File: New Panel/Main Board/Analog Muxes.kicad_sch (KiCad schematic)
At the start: 242 parts, among them J10 Conn_02x07_Odd_Even, J11 Conn_02x07_Odd_Even, J12 Conn_02x07_Odd_Even, J13 Conn_01x03_Pin, J14 Conn_01x03_Pin, J15 Conn_01x03_Pin, J16 Conn_01x03_Pin, J17 Conn_01x03_Pin, J18 Conn_01x03_Pin, J19 Conn_01x03_Pin, J20 Conn_01x03_Pin, J21 Conn_01x03_Pin, J22 Conn_01x03_Pin, J23 Conn_01x03_Pin, J24 Conn_01x03_Pin, J25 Conn_01x03_Pin, J26 Conn_01x03_Pin, J27 Conn_01x03_Pin, J28 Conn_01x03_Pin, J29 Conn_01x03_Pin, J30 Conn_01x03_Pin, J31 Conn_01x03_Pin, J32 Conn_01x03_Pin, J33 Conn_01x03_Pin, J34 Conn_01x03_Pin, J35 Conn_01x03_Pin, J36 Conn_01x03_Pin, J37 Conn_01x03_Pin, J38 Conn_01x03_Pin, J39 Conn_01x03_Pin, J40 Conn_01x03_Pin, J41 Conn_01x03_Pin, J42 Conn_01x03_Pin, J43 Conn_01x03_Pin, J44 Conn_01x03_Pin, J45 Conn_01x03_Pin, J46 Conn_01x03_Pin, J47 Conn_01x03_Pin, J48 Conn_01x03_Pin, J49 Conn_01x03_Pin, J5 Conn_02x07_Odd_Even, J50 Conn_01x03_Pin, J51 Conn_01x03_Pin, J52 Conn_01x03_Pin, J53 Conn_01x03_Pin, J54 Conn_01x03_Pin, J55 Conn_01x03_Pin, J56 Conn_01x03_Pin, J57 Conn_01x03_Pin, J58 Conn_01x03_Pin, J59 Conn_01x03_Pin, J6 Conn_02x07_Odd_Even, J60 Conn_01x03_Pin, J61 Conn_02x07_Odd_Even, J62 Conn_02x07_Odd_Even, J63 Conn_02x07_Odd_Even, J64 Conn_02x07_Odd_Even, J65 Conn_01x03_Pin, J66 Conn_01x03_Pin, J67 Conn_01x03_Pin, J68 Conn_01x03_Pin, J69 Conn_01x03_Pin, J7 Conn_02x07_Odd_Even, J70 Conn_01x03_Pin, J71 Conn_01x03_Pin, J72 Conn_01x03_Pin, J73 Conn_01x03_Pin, J74 Conn_01x03_Pin, J75 Conn_01x03_Pin, J76 Conn_01x03_Pin, J77 Conn_01x03_Pin, J78 Conn_01x03_Pin, J79 Conn_01x03_Pin, J8 Conn_02x07_Odd_Even, J80 Conn_01x03_Pin, J81 Conn_02x07_Odd_Even, J82 Conn_02x07_Odd_Even, J83 Conn_02x07_Odd_Even, J84 Conn_02x07_Odd_Even, J9 Conn_02x07_Odd_Even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

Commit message: adjusted schematic and started PCB Work
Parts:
- removed C12, C13, C14, C15, C16, C17, C18, C19: 10uF, Capacitor_SMD:C_0603_1608Metric_Pad1.08x0.95mm_HandSolder, symbol Device:C
- removed J45, J46, J47, J48, J49, J50, J51, J52, J53, J54, J55, J56, J57, J58, J59, J60, J65, J66, J67, J68, J69, J70, J71, J72, J73, J74, J75, J76, J77, J78, J79, J80: Conn_01x03_Pin, Connector_JST:JST_PH_B3B-PH-K_1x03_P2.00mm_Vertical, symbol Connector:Conn_01x03_Pin
- removed J61, J62, J63, J64, J81, J82, J83, J84: Conn_02x07_Odd_Even, Connector_IDC:IDC-Header_2x07_P2.54mm_Vertical, symbol Connector_Generic:Conn_02x07_Odd_Even
- removed R100, R101, R102, R103, R104, R105, R106, R107, R108, R109, R110, R111, R112, R113, R114, R115, R116, R117, R118, R119, R120, R121, R122, R123, R124, R125, R126, R127, R128, R129, R66, R67, R68, R69, R70, R71, R72, R73, R74, R75, R76, R77, R78, R79, R80, R81, R82, R83, R84, R85, R86, R87, R88, R89, R90, R91, R92, R93, R94, R95, R96, R97, R98, R99: 10K, Resistor_SMD:R_0603_1608Metric, symbol Device:R
- removed U11, U12, U13, U14, U15, U16, U17, U18: Analog_MUX_CD4067BPWR, New Panel Parts:24-TSSOP_(4.4mm), symbol New_Panel_Parts:Analog_MUX_CD4067BPWR
- added D65, D66, D67, D68, D69, D70, D71, D72, D73, D74, D75, D76, D77, D78, D79, D80, D81, D82, D83, D84, D85, D86, D87, D88, D89, D90, D91, D92, D93, D94, D95, D96: DESD5V0S1BA-7, Diode_SMD:D_SOD-323, symbol Diode:SD05_SOD323
- added TP1, TP2, TP3, TP4, TP5, TP6, TP7, TP8: TestPoint, Connector_Pin:Pin_D1.0mm_L10.0mm, symbol Connector:TestPoint
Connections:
- net SW0_0: now also D65.1 (A1)
- net SW0_1: now also J44.2 (Pin_2), D96.1 (A1); no longer J41.2 (Pin_2), U10.9 (CHANNELIN/OUT0)
- net SW10_0: now also D75.1 (A1)
- net SW10_1: now also J34.2 (Pin_2), D86.1 (A1); no longer J35.2 (Pin_2), U10.21 (CHANNELIN/OUT10)
- net SW11_0: now also D76.1 (A1)
- net SW11_1: now also J33.2 (Pin_2), D85.1 (A1); no longer J31.2 (Pin_2), U10.20 (CHANNELIN/OUT11)
- net SW12_0: now also D77.1 (A1)
- net SW12_1: now also J32.2 (Pin_2), D84.1 (A1); no longer J44.2 (Pin_2), U10.19 (CHANNELIN/OUT12)
- net SW13_0: now also D78.1 (A1)
- net SW13_1: now also J31.2 (Pin_2), D83.1 (A1); no longer J40.2 (Pin_2), U10.18 (CHANNELIN/OUT13)
- net SW14_0: now also D79.1 (A1)
- net SW14_1: now also J30.2 (Pin_2), D82.1 (A1); no longer J36.2 (Pin_2), U10.17 (CHANNELIN/OUT14)
- net SW15_0: now also D80.1 (A1)
- net SW15_1: now also J29.2 (Pin_2), D81.1 (A1); no longer J32.2 (Pin_2), U10.16 (CHANNELIN/OUT15)
- net SW1_0: now also D66.1 (A1)
- net SW1_1: now also J43.2 (Pin_2), D95.1 (A1); no longer J37.2 (Pin_2), U10.8 (CHANNELIN/OUT1)
- net SW2_0: now also D67.1 (A1)
- net SW2_1: now also J42.2 (Pin_2), D94.1 (A1); no longer J33.2 (Pin_2), U10.7 (CHANNELIN/OUT2)
- net SW3_0: now also D68.1 (A1)
- net SW3_1: now also J41.2 (Pin_2), D93.1 (A1); no longer J29.2 (Pin_2), U10.6 (CHANNELIN/OUT3)
- net SW4_0: now also D69.1 (A1)
- net SW4_1: now also J40.2 (Pin_2), D92.1 (A1); no longer J42.2 (Pin_2), U10.5 (CHANNELIN/OUT4)
- net SW5_0: now also D70.1 (A1)
- net SW5_1: now also J39.2 (Pin_2), D91.1 (A1); no longer J38.2 (Pin_2), U10.4 (CHANNELIN/OUT5)
- net SW6_0: now also D71.1 (A1)
- net SW6_1: now also J38.2 (Pin_2), D90.1 (A1); no longer J34.2 (Pin_2), U10.3 (CHANNELIN/OUT6)
- net SW7_0: now also D72.1 (A1)
- net SW7_1: now also J37.2 (Pin_2), D89.1 (A1); no longer J30.2 (Pin_2), U10.2 (CHANNELIN/OUT7)
- net SW8_0: now also D73.1 (A1)
- net SW8_1: now also J36.2 (Pin_2), D88.1 (A1); no longer J43.2 (Pin_2), U10.23 (CHANNELIN/OUT8)
- net SW9_0: now also D74.1 (A1)
- net SW9_1: now also J35.2 (Pin_2), D87.1 (A1); no longer J39.2 (Pin_2), U10.22 (CHANNELIN/OUT9)
- net VSS: now also D65.2 (A2), D66.2 (A2), D67.2 (A2), D68.2 (A2), D69.2 (A2), D70.2 (A2), D71.2 (A2), D72.2 (A2), D73.2 (A2), D74.2 (A2), D75.2 (A2), D76.2 (A2), D77.2 (A2), D78.2 (A2), D79.2 (A2), D80.2 (A2), D81.2 (A2), D82.2 (A2), D83.2 (A2), D84.2 (A2), D85.2 (A2), D86.2 (A2), D87.2 (A2), D88.2 (A2), D89.2 (A2), D90.2 (A2), D91.2 (A2), D92.2 (A2), D93.2 (A2), D94.2 (A2), D95.2 (A2), D96.2 (A2)
- net at U10.1 (COMMONOUT/IN): now also U2.5 (CHANNELIN/OUT4); no longer U2.2 (CHANNELIN/OUT7)
- net at U2.23 (CHANNELIN/OUT8): now also TP1.1
- net at U2.21 (CHANNELIN/OUT10): now also TP3.1
- net at U8.1 (COMMONOUT/IN): now also U2.3 (CHANNELIN/OUT6); no longer U2.4 (CHANNELIN/OUT5)
- net at U9.1 (COMMONOUT/IN): now also U2.2 (CHANNELIN/OUT7); no longer U2.3 (CHANNELIN/OUT6)
- net at U2.16 (CHANNELIN/OUT15): now also TP8.1
- net at U2.17 (CHANNELIN/OUT14): now also TP7.1
- net at U2.18 (CHANNELIN/OUT13): now also TP6.1
- net at U2.19 (CHANNELIN/OUT12): now also TP5.1
- net at U2.20 (CHANNELIN/OUT11): now also TP4.1
- net at U2.22 (CHANNELIN/OUT9): now also TP2.1
- net at U7.1 (COMMONOUT/IN): now also U2.4 (CHANNELIN/OUT5); no longer U2.5 (CHANNELIN/OUT4)
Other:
- moved on the sheet: C10, C11, C20, C4, C5, C6, C7, C8, C9, J10, J11, J12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

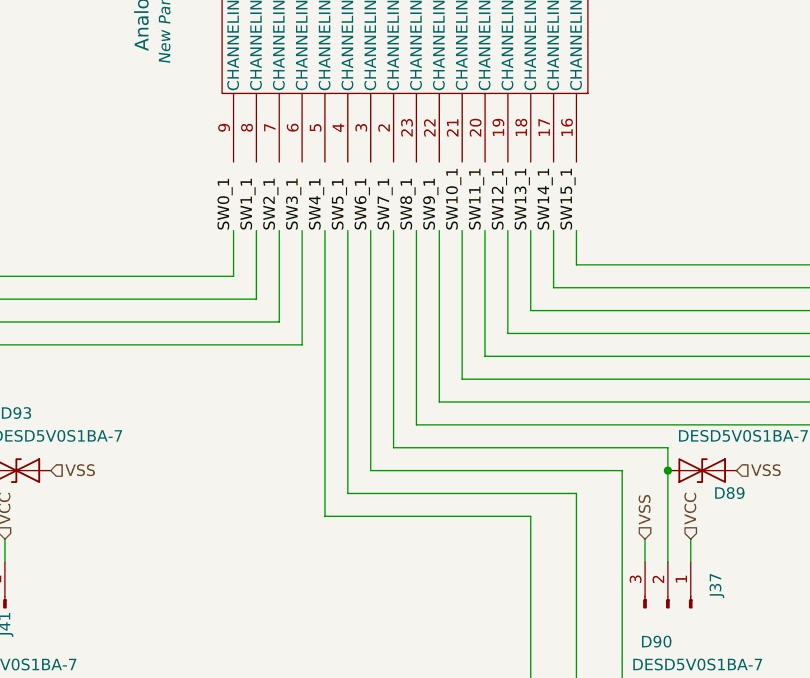
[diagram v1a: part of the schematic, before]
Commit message: Continued PCB Layout
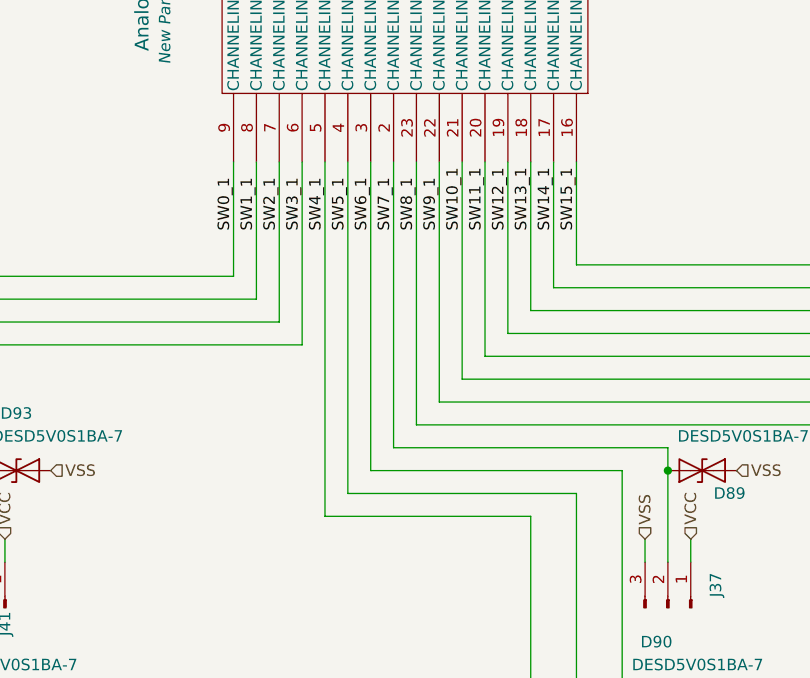
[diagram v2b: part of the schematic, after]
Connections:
- net SW0_1: now also U10.9 (CHANNELIN/OUT0)
- net SW10_1: now also U10.21 (CHANNELIN/OUT10)
- net SW11_1: now also U10.20 (CHANNELIN/OUT11)
- net SW12_1: now also U10.19 (CHANNELIN/OUT12)
- net SW13_1: now also U10.18 (CHANNELIN/OUT13)
- net SW14_1: now also U10.17 (CHANNELIN/OUT14)
- net SW15_1: now also U10.16 (CHANNELIN/OUT15)
- net SW1_1: now also U10.8 (CHANNELIN/OUT1)
- net SW2_1: now also U10.7 (CHANNELIN/OUT2)
- net SW3_1: now also U10.6 (CHANNELIN/OUT3)
- net SW4_1: now also U10.5 (CHANNELIN/OUT4)
- net SW5_1: now also U10.4 (CHANNELIN/OUT5)
- net SW6_1: now also U10.3 (CHANNELIN/OUT6)
- net SW7_1: now also U10.2 (CHANNELIN/OUT7)
- net SW8_1: now also U10.23 (CHANNELIN/OUT8)
- net SW9_1: now also U10.22 (CHANNELIN/OUT9)
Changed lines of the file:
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@@
 		(title "Main Universal Panel Board")
 		(date "2025-08-06")
-		(rev "X0")
+		(rev "X1")
 		(company "CMSC")
 		(comment 1 "NF 2025")
@@
 	(wire
 		(pts
-			(xy 394.97 234.95) (xy 394.97 241.3)
+			(xy 394.97 227.33) (xy 394.97 241.3)
 		)
 		(stroke
@@
 	(wire
 		(pts
+			(xy 379.73 227.33) (xy 379.73 256.54)
+		)
+		(stroke
+			(width 0)
+			(type default)
+		)
+	)
+	(wire
+		(pts
 			(xy 562.61 269.24) (xy 562.61 271.78)
 		)
@@
 	(wire
 		(pts
-			(xy 379.73 234.95) (xy 379.73 256.54)
-		)
-		(stroke
-			(width 0)
-			(type default)
-		)
-	)
-	(wire
-		(pts
 			(xy 307.34 149.86) (xy 165.1 149.86)
 		)
@@
 	(wire
 		(pts
-			(xy 387.35 234.95) (xy 387.35 248.92)
+			(xy 387.35 227.33) (xy 387.35 248.92)
 		)
 		(stroke
@@
 	(wire
 		(pts
-			(xy 361.95 234.95) (xy 361.95 242.57)
+			(xy 361.95 227.33) (xy 361.95 242.57)
 		)
 		(stroke
@@
 	(wire
 		(pts
-			(xy 389.89 234.95) (xy 389.89 246.38)
-		)
-		(stroke
-			(width 0)
-			(type default)
-		)
-	)
-	(wire
-		(pts
 			(xy 220.98 246.38) (xy 66.04 246.38)
 		)
@@
 	(wire
 		(pts
+			(xy 369.57 227.33) (xy 369.57 266.7)
+		)
+		(stroke
+			(width 0)
+			(type default)
+		)
+	)
+	(wire
+		(pts
 			(xy 337.82 93.98) (xy 337.82 83.82)
 		)
@@
 	(wire
 		(pts
-			(xy 359.41 234.95) (xy 359.41 240.03)
+			(xy 359.41 227.33) (xy 359.41 240.03)
 		)
 		(stroke
@@
 	(wire
 		(pts
-			(xy 374.65 234.95) (xy 374.65 261.62)
+			(xy 374.65 227.33) (xy 374.65 261.62)
 		)
 		(stroke
@@
 	(wire
 		(pts
-			(xy 372.11 234.95) (xy 372.11 264.16)
+			(xy 372.11 227.33) (xy 372.11 264.16)
 		)
 		(stroke
@@
 	(wire
 		(pts
-			(xy 367.03 234.95) (xy 367.03 247.65)
+			(xy 367.03 227.33) (xy 367.03 247.65)
 		)
 		(stroke
@@
 	(wire
 		(pts
-			(xy 397.51 238.76) (xy 397.51 234.95)
+			(xy 397.51 227.33) (xy 397.51 238.76)
 		)
 		(stroke
@@
 	(wire
 		(pts
-			(xy 377.19 234.95) (xy 377.19 259.08)
+			(xy 377.19 227.33) (xy 377.19 259.08)
 		)
 		(stroke
@@
 	(wire
 		(pts
-			(xy 364.49 234.95) (xy 364.49 245.11)
+			(xy 364.49 227.33) (xy 364.49 245.11)
 		)
 		(stroke
@@
 	(wire
 		(pts
-			(xy 382.27 234.95) (xy 382.27 254)
+			(xy 382.27 227.33) (xy 382.27 254)
 		)
 		(stroke
@@
 	(wire
 		(pts
-			(xy 384.81 234.95) (xy 384.81 251.46)
+			(xy 384.81 227.33) (xy 384.81 251.46)
 		)
 		(stroke
@@
 	(wire
 		(pts
-			(xy 369.57 234.95) (xy 369.57 266.7)
-		)
-		(stroke
-			(width 0)
-			(type default)
-		)
-	)
-	(wire
-		(pts
 			(xy 231.14 227.33) (xy 231.14 256.54)
 		)
@@
 	(wire
 		(pts
+			(xy 389.89 227.33) (xy 389.89 246.38)
+		)
+		(stroke
+			(width 0)
+			(type default)
+		)
+	)
+	(wire
+		(pts
 			(xy 295.91 25.4) (xy 298.45 25.4)
 		)
@@
 	(wire
 		(pts
-			(xy 392.43 234.95) (xy 392.43 243.84)
+			(xy 392.43 227.33) (xy 392.43 243.84)
 		)
 		(stroke
